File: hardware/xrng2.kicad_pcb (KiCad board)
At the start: 4 copper layers, 70 x 60 mm, 71 parts, among them J101 AVR-PDI-6A, J102 GS3, J103 GS3, J104 Conn_01x02, J105 Conn_01x03, J106 Conn_01x02, J107 USB_B, J301 GS2, Q301 MMBT3904, Q302 MMBT3904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

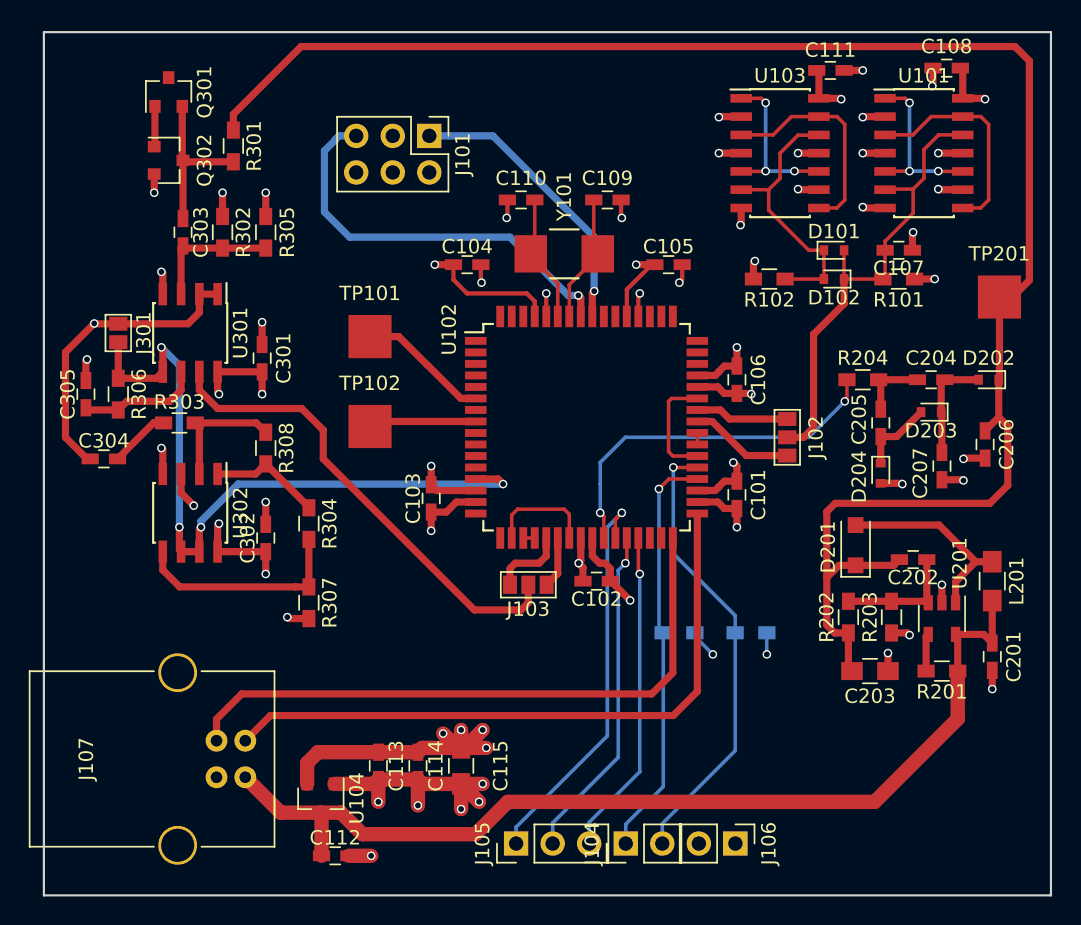
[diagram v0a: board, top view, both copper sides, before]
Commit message: Mounting holes
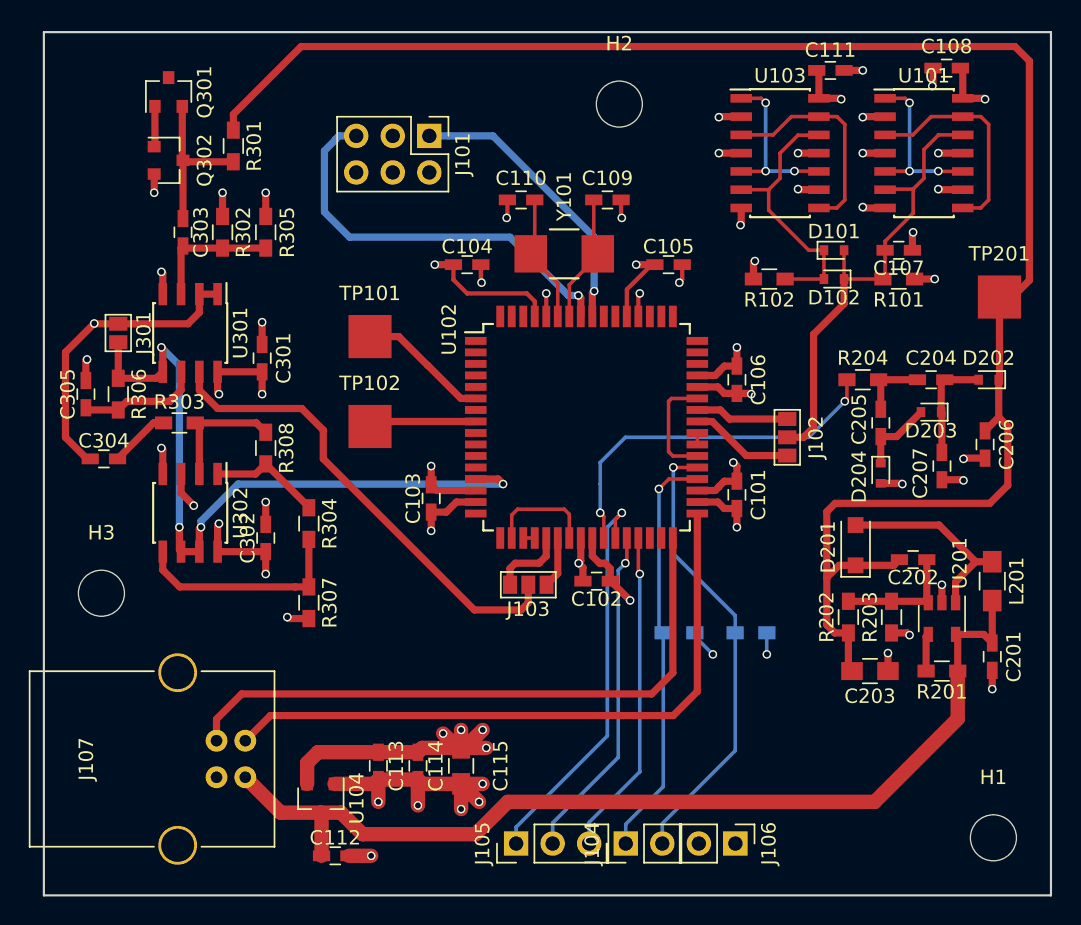
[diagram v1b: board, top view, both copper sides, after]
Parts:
- added H1: MOUNT, Mounting_Holes:MountingHole_3.2mm_M3, F.Cu at (106.0, 116.0)
- added H2: MOUNT, Mounting_Holes:MountingHole_3.2mm_M3, F.Cu at (80.0, 65.0)
- added H3: MOUNT, Mounting_Holes:MountingHole_3.2mm_M3, F.Cu at (44.0, 99.0)
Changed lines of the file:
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@@
 (kicad_pcb (version 4) (host pcbnew 4.0.7)
   (general
-    (links 177)
+    (links 180)
     (no_connects 0)
     (area 39.924999 59.924999 110.075001 120.075001)
@@
     (tracks 548)
     (zones 0)
-    (modules 71)
+    (modules 74)
     (nets 50)
   )
@@
     )
   )
+  (module Mounting_Holes:MountingHole_3.2mm_M3 (layer F.Cu)
+    (at 106 116)
+    (descr "Mounting Hole 3.2mm, no annular, M3")
+    (tags "mounting hole 3.2mm no annular m3")
+    (attr virtual)
+    (fp_text reference H1 (at 0 -4.2) (layer F.SilkS)
+      (effects (font (size 1 1) (thickness 0.15)))
+    )
+    (fp_text value MOUNT (at 0 4.2) (layer F.Fab)
+      (effects (font (size 1 1) (thickness 0.15)))
+    )
+    (fp_text user %R (at 0.3 0) (layer F.Fab)
+      (effects (font (size 1 1) (thickness 0.15)))
+    )
+    (fp_circle (center 0 0) (end 3.2 0) (layer Cmts.User) (width 0.15))
+    (fp_circle (center 0 0) (end 3.45 0) (layer F.CrtYd) (width 0.05))
+    (pad 1 np_thru_hole circle (at 0 0) (size 3.2 3.2) (drill 3.2) (layers *.Cu *.Mask)
+      (net 2 GND))
+  )
+  (module Mounting_Holes:MountingHole_3.2mm_M3 (layer F.Cu)
+    (at 80 65)
+    (descr "Mounting Hole 3.2mm, no annular, M3")
+    (tags "mounting hole 3.2mm no annular m3")
+    (attr virtual)
+    (fp_text reference H2 (at 0 -4.2) (layer F.SilkS)
+      (effects (font (size 1 1) (thickness 0.15)))
+    )
+    (fp_text value MOUNT (at 0 4.2) (layer F.Fab)
+      (effects (font (size 1 1) (thickness 0.15)))
+    )
+    (fp_text user %R (at 0.3 0) (layer F.Fab)
+      (effects (font (size 1 1) (thickness 0.15)))
+    )
+    (fp_circle (center 0 0) (end 3.2 0) (layer Cmts.User) (width 0.15))
+    (fp_circle (center 0 0) (end 3.45 0) (layer F.CrtYd) (width 0.05))
+    (pad 1 np_thru_hole circle (at 0 0) (size 3.2 3.2) (drill 3.2) (layers *.Cu *.Mask)
+      (net 2 GND))
+  )
+  (module Mounting_Holes:MountingHole_3.2mm_M3 (layer F.Cu)
+    (at 44 99)
+    (descr "Mounting Hole 3.2mm, no annular, M3")
+    (tags "mounting hole 3.2mm no annular m3")
+    (attr virtual)
+    (fp_text reference H3 (at 0 -4.2) (layer F.SilkS)
+      (effects (font (size 1 1) (thickness 0.15)))
+    )
+    (fp_text value MOUNT (at 0 4.2) (layer F.Fab)
+      (effects (font (size 1 1) (thickness 0.15)))
+    )
+    (fp_text user %R (at 0.3 0) (layer F.Fab)
+      (effects (font (size 1 1) (thickness 0.15)))
+    )
+    (fp_circle (center 0 0) (end 3.2 0) (layer Cmts.User) (width 0.15))
+    (fp_circle (center 0 0) (end 3.45 0) (layer F.CrtYd) (width 0.05))
+    (pad 1 np_thru_hole circle (at 0 0) (size 3.2 3.2) (drill 3.2) (layers *.Cu *.Mask)
+      (net 2 GND))
+  )
   (gr_line (start 60.6 117.9) (end 59.9 117.9) (layer Eco1.User) (width 0.2))

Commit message: Layer IDs
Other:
- board text added: "2"
- board text added: "3"
- board text added: "4"
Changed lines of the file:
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@@
     (area 39.924999 59.924999 110.075001 120.075001)
     (thickness 1.6)
-    (drawings 284)
+    (drawings 288)
     (tracks 548)
     (zones 0)
@@
       (net 2 GND))
   )
+  (gr_text 4 (at 101 118) (layer B.Cu)
+    (effects (font (size 1.5 1.5) (thickness 0.3)) (justify mirror))
+  )
+  (gr_text 3 (at 99 118) (layer GND)
+    (effects (font (size 1.5 1.5) (thickness 0.3)))
+  )
+  (gr_text 2 (at 97 118) (layer PWR)
+    (effects (font (size 1.5 1.5) (thickness 0.3)))
+  )
+  (gr_text 1 (at 95 118) (layer F.Cu)
+    (effects (font (size 1.5 1.5) (thickness 0.3)))
+  )
   (gr_line (start 60.6 117.9) (end 59.9 117.9) (layer Eco1.User) (width 0.2))
   (gr_line (start 59.9 116.6) (end 60.6 116.6) (layer Eco1.User) (width 0.2))
@@
     (polygon
       (pts
-        (xy 40 60) (xy 110 60) (xy 110 120) (xy 40 120)
+        (xy 40 60) (xy 110 60) (xy 110 120) (xy 103 120) (xy 103 116)
+        (xy 93 116) (xy 93 120) (xy 40 120)
       )
     )
@@
     (polygon
       (pts
-        (xy 75 60) (xy 110 60) (xy 110 120) (xy 40 120) (xy 40 60)
+        (xy 75 60) (xy 110 60) (xy 110 120) (xy 103 120) (xy 103 116)
+        (xy 93 116) (xy 93 120) (xy 40 120) (xy 40 60)
       )
     )

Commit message: ident text
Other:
- board text added: "xrng2 eval 06/2018 kuro68k"
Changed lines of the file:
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@@
     (area 39.924999 59.924999 110.075001 120.075001)
     (thickness 1.6)
-    (drawings 288)
+    (drawings 289)
     (tracks 548)
     (zones 0)
@@
       (net 2 GND))
   )
+  (gr_text "xrng2 eval\n06/2018\nkuro68k" (at 92 112) (layer Eco1.User)
+    (effects (font (size 1.2 1.2) (thickness 0.2)) (justify left))
+  )
   (gr_text 4 (at 101 118) (layer B.Cu)

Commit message: Additional silk
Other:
- board text added: "+"
- board text added: "-"
- board text added: "G"
- board text added: "M3 GND"
- board text added: "V"
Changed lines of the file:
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@@
     (links 180)
     (no_connects 0)
-    (area 39.924999 59.924999 110.075001 120.075001)
+    (area 38.524999 59.825 134.85 139.83167)
     (thickness 1.6)
-    (drawings 289)
+    (drawings 305)
     (tracks 548)
     (zones 0)
@@
     (visible_elements 7FFCFFFF)
     (pcbplotparams
-      (layerselection 0x00030_80000001)
-      (usegerberextensions false)
+      (layerselection 0x01cc0_80000007)
+      (usegerberextensions true)
       (excludeedgelayer true)
       (linewidth 0.100000)
@@
       (plotinvisibletext false)
       (padsonsilk false)
-      (subtractmaskfromsilk false)
+      (subtractmaskfromsilk true)
       (outputformat 1)
       (mirror false)
       (drillshape 0)
       (scaleselection 1)
-      (outputdirectory ""))
+      (outputdirectory plot/))
   )
   (net 0 "")
@@
       (net 2 GND))
   )
+  (gr_line (start 62 92) (end 59 89) (layer Eco1.User) (width 0.2))
+  (gr_line (start 62 102) (end 62 92) (layer Eco1.User) (width 0.2))
+  (gr_line (start 59 74) (end 59 89) (layer Eco1.User) (width 0.2))
+  (gr_line (start 93 93) (end 109 93) (layer Eco1.User) (width 0.2))
+  (gr_line (start 87 80) (end 103 80) (layer Eco1.User) (width 0.2))
+  (gr_line (start 87 75) (end 87 80) (layer Eco1.User) (width 0.2))
+  (gr_line (start 85 73) (end 87 75) (layer Eco1.User) (width 0.2))
+  (gr_line (start 85 62) (end 85 73) (layer Eco1.User) (width 0.2))
+  (gr_circle (center 106 116) (end 103 114) (layer Eco1.User) (width 0.2))
+  (gr_circle (center 44 99) (end 47 97) (layer Eco1.User) (width 0.2))
+  (gr_circle (center 80 65) (end 77 63) (layer Eco1.User) (width 0.2))
+  (gr_text "M3\nGND" (at 74 64) (layer Eco1.User)
+    (effects (font (size 1.2 1.2) (thickness 0.2)))
+  )
+  (gr_text V (at 54 114) (layer Eco2.User)
+    (effects (font (size 1.5 1.5) (thickness 0.3)))
+  )
+  (gr_text G (at 52 114) (layer Eco2.User)
+    (effects (font (size 1.5 1.5) (thickness 0.3)) (justify mirror))
+  )
+  (gr_text + (at 54 107) (layer Eco2.User)
+    (effects (font (size 1.5 1.5) (thickness 0.3)))
+  )
+  (gr_text - (at 52 107) (layer Eco2.User)
+    (effects (font (size 1.5 1.5) (thickness 0.3)))
+  )
   (gr_text "xrng2 eval\n06/2018\nkuro68k" (at 92 112) (layer Eco1.User)
